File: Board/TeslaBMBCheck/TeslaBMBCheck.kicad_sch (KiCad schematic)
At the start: 0 parts

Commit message: Board & schematic
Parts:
- added C1, C3, C4: 100n, Capacitor_SMD:C_0805_2012Metric, symbol Device:C
- added C15, C17: 22p, Capacitor_SMD:C_0805_2012Metric, symbol Device:C
- added C2: 10u, Capacitor_SMD:C_1206_3216Metric, symbol Device:C
- added C5: 1u, Capacitor_SMD:C_0805_2012Metric, symbol Device:C
- added C6: 47n, Capacitor_SMD:C_0805_2012Metric, symbol Device:C
- added D15: INFO, LED_SMD:LED_0805_2012Metric, symbol Device:LED
- added DS1: WC1602A, spetry:LCD-20x4, symbol Display_Character:WC1602A
- added J1: TESLA_BMS, spetry:Molex_Mini-Fit_Jr_5566-10A_1x05_P4.20mm_Vertical, symbol Connector_Generic:Conn_01x05
- added J9: ICSP, Connector_PinHeader_2.54mm:PinHeader_1x05_P2.54mm_Vertical, symbol Connector_Generic:Conn_01x05
- added Q1: IRLML2244, Package_TO_SOT_SMD:SOT-23, symbol Transistor_FET:IRLML5203
- added Q2: BSS138, Package_TO_SOT_SMD:SOT-23, symbol Transistor_FET:BSS138
- added R1, R2: 5K1, Resistor_SMD:R_0805_2012Metric, symbol Device:R
- added R10: 22K, Resistor_SMD:R_0805_2012Metric, symbol Device:R
- added R19: 1K, Resistor_SMD:R_0805_2012Metric, symbol Device:R
- added R23, R8: 10K, Resistor_SMD:R_0805_2012Metric, symbol Device:R
- added R3, R4, R5: 4K7, Resistor_SMD:R_0805_2012Metric, symbol Device:R
- added R6: 22, Resistor_SMD:R_0805_2012Metric, symbol Device:R
- added RV1: 10K, Potentiometer_SMD:Potentiometer_Bourns_TC33X_Vertical, symbol info_board-rescue:R_POT_TRIM-Device
- added SW1, SW2: ~, Button_Switch_SMD:SW_SPST_CK_RS282G05A3, symbol Switch:SW_Push
- added U1: USBLC6, Package_TO_SOT_SMD:SOT-23-6, symbol Power_Protection:USBLC6-2SC6
- added U2: PIC18F2480-ISO, Package_SO:SOIC-28W_7.5x17.9mm_P1.27mm, symbol spetry:PIC18F2480-ISO
- added USB1: POWER, spetry:HRO-TYPE-C-31-M-12, symbol backplane-rescue:HRO-TYPE-C-31-M-12-Type-C
- added Y1: 10 MHz, Crystal:Crystal_SMD_HC49-SD, symbol Device:Crystal
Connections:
- new net: R10.1, RV1.1
- new net: DS1.3 (VO), RV1.2
- new net: DS1.16 (LED(-)), Q2.3 (D)
- new net: C5.1, Q1.2 (S), R6.1
- new net: D15.2 (A), R19.2
- new net: C4.1, R3.1, SW2.1, U2.3 (RA1/AN1)
- new net: C3.1, R4.1, SW1.1, U2.2 (RA0/AN0)
- new net: D15.1 (K), U2.13 (CCP1/RC2)
- new net BACKLT: Q2.1 (G), R8.1, U2.12 (T1OSI/RC1)
- new net BMS_FAULT: J1.5 (Pin_5), R5.2
- new net BMS_POWER_ON: Q1.1 (G), U2.11 (T1OSO/T13CKI/RC0)
- new net BMS_RX: J1.2 (Pin_2), U1.3 (I/O2)
- new net BMS_TX: J1.3 (Pin_3), U1.1 (I/O1)
- new net BMS_VCC: C6.1, J1.1 (Pin_1), Q1.3 (D), R5.1
- new net CC1: R2.1, USB1.4 (CC1)
- new net CC2: R1.1, USB1.10 (CC2)
- new net GND: C1.2, C15.2, C17.2, C2.1, C3.2, C4.2, C5.2, C6.2, DS1.1 (VSS), DS1.10 (D3), DS1.5 (R/W), DS1.7 (D0), DS1.8 (D1), DS1.9 (D2), J1.4 (Pin_4), J9.3 (Pin_3), Q2.2 (S), R1.2, R2.2, R8.2, RV1.3, SW1.2, SW2.2, U1.2 (GND), U2.19 (VSS), U2.8 (VSS), USB1.1 (GND), USB1.12 (GND), USB1.13 (SHIELD)
- new net LCD_D4: DS1.11 (D4), U2.21 (RB0/INT0/AN10)
- new net LCD_D5: DS1.12 (D5), U2.22 (RB1/INT1/AN8)
- new net LCD_D6: DS1.13 (D6), U2.23 (RB2/AN8/INT2/CANTX)
- new net LCD_D7: DS1.14 (D7), U2.24 (RB3/CANRX)
- new net LCD_E: DS1.4 (RS), U2.25 (RB4/KBI0/AN9)
- new net LCD_RS: DS1.6 (E), U2.26 (RB5/KBI1/PGM)
- new net OSC1: C17.1, U2.9 (RA7/OSC1/CLKI), Y1.1
- new net OSC2: C15.1, U2.10 (RA6/OSC2/CLKO), Y1.2
- new net PGC: J9.5 (Pin_5), U2.27 (RB6/KBI2/PGC)
- new net PGD: J9.4 (Pin_4), U2.28 (RB7/KBI3/PGD)
- new net RX: U1.4 (I/O2), U2.18 (RX/DT/RC7)
- new net TX: U1.6 (I/O1), U2.17 (TX/CK/RC6)
- new net VCC: C1.1, C2.2, DS1.15 (LED(+)), DS1.2 (VDD), J9.2 (Pin_2), R10.2, R19.1, R23.1, R3.2, R4.2, R6.2, U1.5 (VBUS), U2.20 (VDD), USB1.11 (VBUS), USB1.2 (VBUS)
- new net VPP: J9.1 (Pin_1), R23.2, U2.1 (Vpp/~{MCLR}/RE3)
- no-connect marks 0 -> 13

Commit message: Change info LED connection
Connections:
- net GND: now also D15.1 (K)
- net VCC: no longer R19.1
- net at U2.13 (CCP1/RC2): now also R19.1; no longer D15.1 (K)
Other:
- title: (none) -> TeslaBMBChecker
- moved on the sheet: D15, R19
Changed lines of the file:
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@@
 	(generator_version "9.0")
 	(paper "A4")
+	(title_block
+		(title "TeslaBMBChecker")
+		(date "2025-07-10")
+		(rev "0.1")
+	)
 	(junction
 		(at 45.72 181.61)
@@
 	(wire
 		(pts
+			(xy 99.06 96.52) (xy 99.06 58.42)
+		)
+		(stroke
+			(width 0)
+			(type default)
+		)
+	)
+	(wire
+		(pts
 			(xy 176.53 57.15) (xy 176.53 44.45)
 		)
@@
 	(wire
 		(pts
+			(xy 88.9 58.42) (xy 88.9 62.23)
+		)
+		(stroke
+			(width 0)
+			(type default)
+		)
+	)
+	(wire
+		(pts
 			(xy 234.95 104.14) (xy 231.14 104.14)
 		)
@@
 	(wire
 		(pts
-			(xy 255.27 99.06) (xy 274.32 99.06)
+			(xy 99.06 58.42) (xy 88.9 58.42)
 		)
 		(stroke
@@
 	(wire
 		(pts
-			(xy 274.32 69.85) (xy 274.32 71.12)
+			(xy 255.27 99.06) (xy 274.32 99.06)
 		)
 		(stroke
@@
 	(wire
 		(pts
-			(xy 176.53 35.56) (xy 168.91 35.56)
+			(xy 274.32 69.85) (xy 274.32 71.12)
 		)
 		(stroke
@@
 	(wire
 		(pts
-			(xy 231.14 106.68) (xy 234.95 106.68)
+			(xy 176.53 35.56) (xy 168.91 35.56)
 		)
 		(stroke
@@
 	(wire
 		(pts
-			(xy 99.06 96.52) (xy 102.87 96.52)
+			(xy 231.14 106.68) (xy 234.95 106.68)
 		)
 		(stroke
@@
 	(wire
 		(pts
-			(xy 99.06 80.01) (xy 99.06 96.52)
+			(xy 99.06 96.52) (xy 102.87 96.52)
 		)
 		(stroke
@@
 	)
 	(symbol
-		(lib_id "power:VCC")
-		(at 99.06 64.77 0)
+		(lib_id "power:GND")
+		(at 88.9 77.47 0)
 		(unit 1)
 		(exclude_from_sim no)
@@
 		(on_board yes)
 		(dnp no)
-		(fields_autoplaced yes)
 		(property "Reference" "#PWR022"
-			(at 99.06 68.58 0)
+			(at 88.9 83.82 0)
 			(effects
 				(font
@@
 			)
 		)
-		(property "Value" "VCC"
-			(at 99.06 59.69 0)
+		(property "Value" "GND"
+			(at 88.9 81.788 0)
 			(effects
 				(font
@@
 		)
 		(property "Footprint" ""
-			(at 99.06 64.77 0)
+			(at 88.9 77.47 0)
 			(effects
 				(font
@@
 		)
 		(property "Datasheet" ""
-			(at 99.06 64.77 0)
+			(at 88.9 77.47 0)
 			(effects
 				(font
@@
 			)
 		)
-		(property "Description" "Power symbol creates a global label with name \"VCC\""
-			(at 99.06 64.77 0)
+		(property "Description" "Power symbol creates a global label with name \"GND\" , ground"
+			(at 88.9 77.47 0)
 			(effects
 				(font
@@
 	(symbol
 		(lib_id "Device:R")
-		(at 99.06 68.58 0)
+		(at 88.9 66.04 0)
 		(unit 1)
 		(exclude_from_sim no)
@@
 		(dnp no)
 		(property "Reference" "R19"
-			(at 100.838 67.4116 0)
+			(at 90.678 64.8716 0)
 			(effects
 				(font
@@
 		)
 		(property "Value" "1K"
-			(at 100.838 69.723 0)
+			(at 90.678 67.183 0)
 			(effects
 				(font
@@
 		)
 		(property "Footprint" "Resistor_SMD:R_0805_2012Metric"
-			(at 97.282 68.58 90)
+			(at 87.122 66.04 90)
 			(effects
 				(font
@@
 		)
 		(property "Datasheet" "~"
-			(at 99.06 68.58 0)
+			(at 88.9 66.04 0)
 			(effects
 				(font
@@
 		)
 		(property "Description" ""
-			(at 99.06 68.58 0)
+			(at 88.9 66.04 0)
 			(effects
 				(font
@@
 	(symbol
 		(lib_id "Device:LED")
-		(at 99.06 76.2 90)
+		(at 88.9 73.66 90)
 		(unit 1)
 		(exclude_from_sim no)
@@
 		(dnp no)
 		(property "Reference" "D15"
-			(at 102.0572 75.2094 90)
+			(at 91.8972 72.6694 90)
 			(effects
 				(font
@@
 		)
 		(property "Value" "INFO"
-			(at 102.0572 77.5208 90)
+			(at 91.8972 74.9808 90)
 			(effects
 				(font
@@
 		)
 		(property "Footprint" "LED_SMD:LED_0805_2012Metric"
-			(at 99.06 76.2 0)
+			(at 88.9 73.66 0)
 			(effects
 				(font
@@
 		)
 		(property "Datasheet" "~"
-			(at 99.06 76.2 0)
+			(at 88.9 73.66 0)
 			(effects
 				(font
@@
 		)
 		(property "Description" ""
-			(at 99.06 76.2 0)
+			(at 88.9 73.66 0)
 			(effects
 				(font

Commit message: Layout improvements
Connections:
- net LCD_E: now also DS1.6 (E), U2.26 (RB5/KBI1/PGM); no longer DS1.4 (RS), U2.25 (RB4/KBI0/AN9)
- net LCD_RS: now also DS1.4 (RS), U2.25 (RB4/KBI0/AN9); no longer DS1.6 (E), U2.26 (RB5/KBI1/PGM)
- net LED-: now reaches DS1.16 (LED(-)), Q2.3 (D)
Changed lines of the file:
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@@
+		)
+	)
+	(label "LED-"
+		(at 257.81 101.6 0)
+		(effects
+			(font
+				(size 1.27 1.27)
+			)
+			(justify left bottom)
 		)
 	)
@@
 	)
 	(label "LCD_RS"
-		(at 207.01 127 0)
+		(at 207.01 124.46 0)
 		(effects
 			(font
@@
 	)
 	(label "LCD_E"
-		(at 207.01 124.46 0)
+		(at 207.01 127 0)
 		(effects
 			(font
@@
 		(effects
 			(font
+				(size 1.27 1.27)
+			)
+			(justify left bottom)
+		)
+	)
+	(label "LED+"
+		(at 257.81 99.06 0)
+		(effects
+			(font

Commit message: Final fixes. Created Gerber files.
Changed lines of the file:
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@@
 	(title_block
 		(title "TeslaBMBChecker")
-		(date "2025-07-10")
-		(rev "0.1")
+		(date "2025-07-11")
+		(rev "1.0")
 	)
 	(junction
@@
 		(effects
 			(font
-				(size 1.27 1.27)
-			)
-			(justify left bottom)
-		)
-	)
-	(label "LED+"
-		(at 257.81 99.06 0)
-		(effects
-			(font

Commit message: Fixes swapped RX/TX. Changes R10 value
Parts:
- R10: value 22K -> 15K
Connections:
- net BMS_RX: now also J1.3 (Pin_3), U1.1 (I/O1); no longer J1.2 (Pin_2), U1.3 (I/O2)
- net BMS_TX: now also J1.2 (Pin_2), U1.3 (I/O2); no longer J1.3 (Pin_3), U1.1 (I/O1)
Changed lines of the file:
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@@
 	(title_block
 		(title "TeslaBMBChecker")
-		(date "2025-07-11")
-		(rev "1.0")
+		(date "2025-07-26")
+		(rev "1.1")
 	)
 	(junction
@@
 	)
 	(label "BMS_RX"
-		(at 30.48 109.22 0)
+		(at 30.48 106.68 0)
 		(effects
 			(font
@@
 	)
 	(label "BMS_TX"
-		(at 30.48 106.68 0)
+		(at 30.48 109.22 0)
 		(effects
 			(font
@@
 			)
 		)
-		(property "Value" "22K"
+		(property "Value" "15K"
 			(at 267.1064 76.2 90)
 			(effects

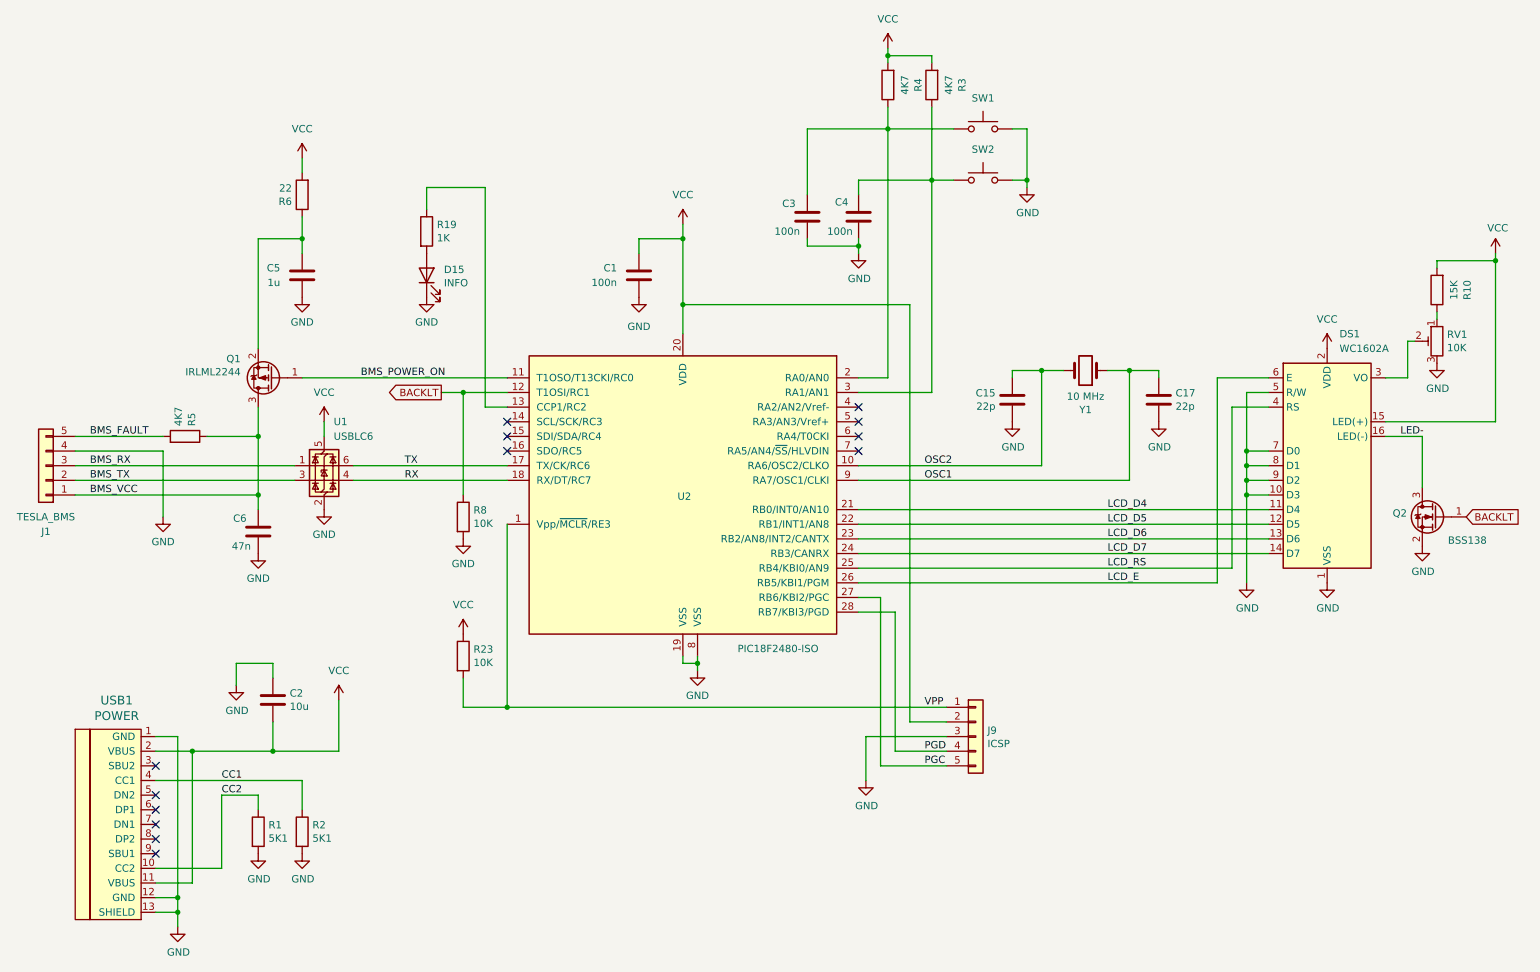
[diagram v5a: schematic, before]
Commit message: Adds fault detection and clearing.
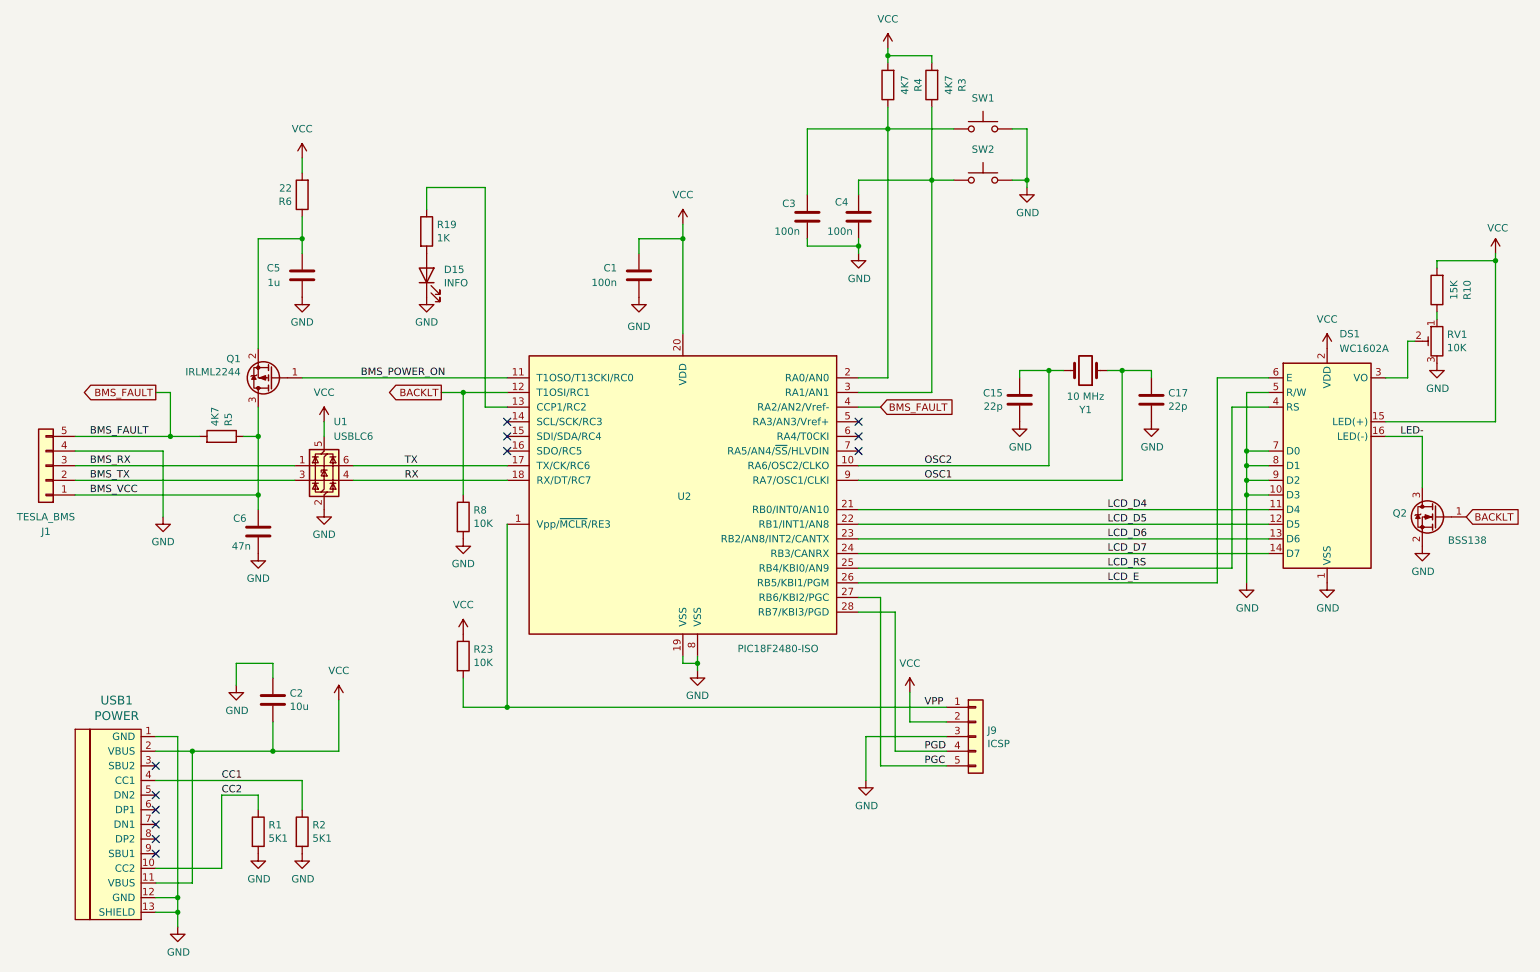
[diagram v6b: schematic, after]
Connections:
- net BMS_FAULT: now also U2.4 (RA2/AN2/Vref-)
- no-connect marks 13 -> 12
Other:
- moved on the sheet: C15, C17, R5
